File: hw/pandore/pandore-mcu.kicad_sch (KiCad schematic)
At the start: 33 parts, among them U3 RP2350B, U5 mem_flash_spi, X1 ${F}, ${tol}+${stab}, ${load}

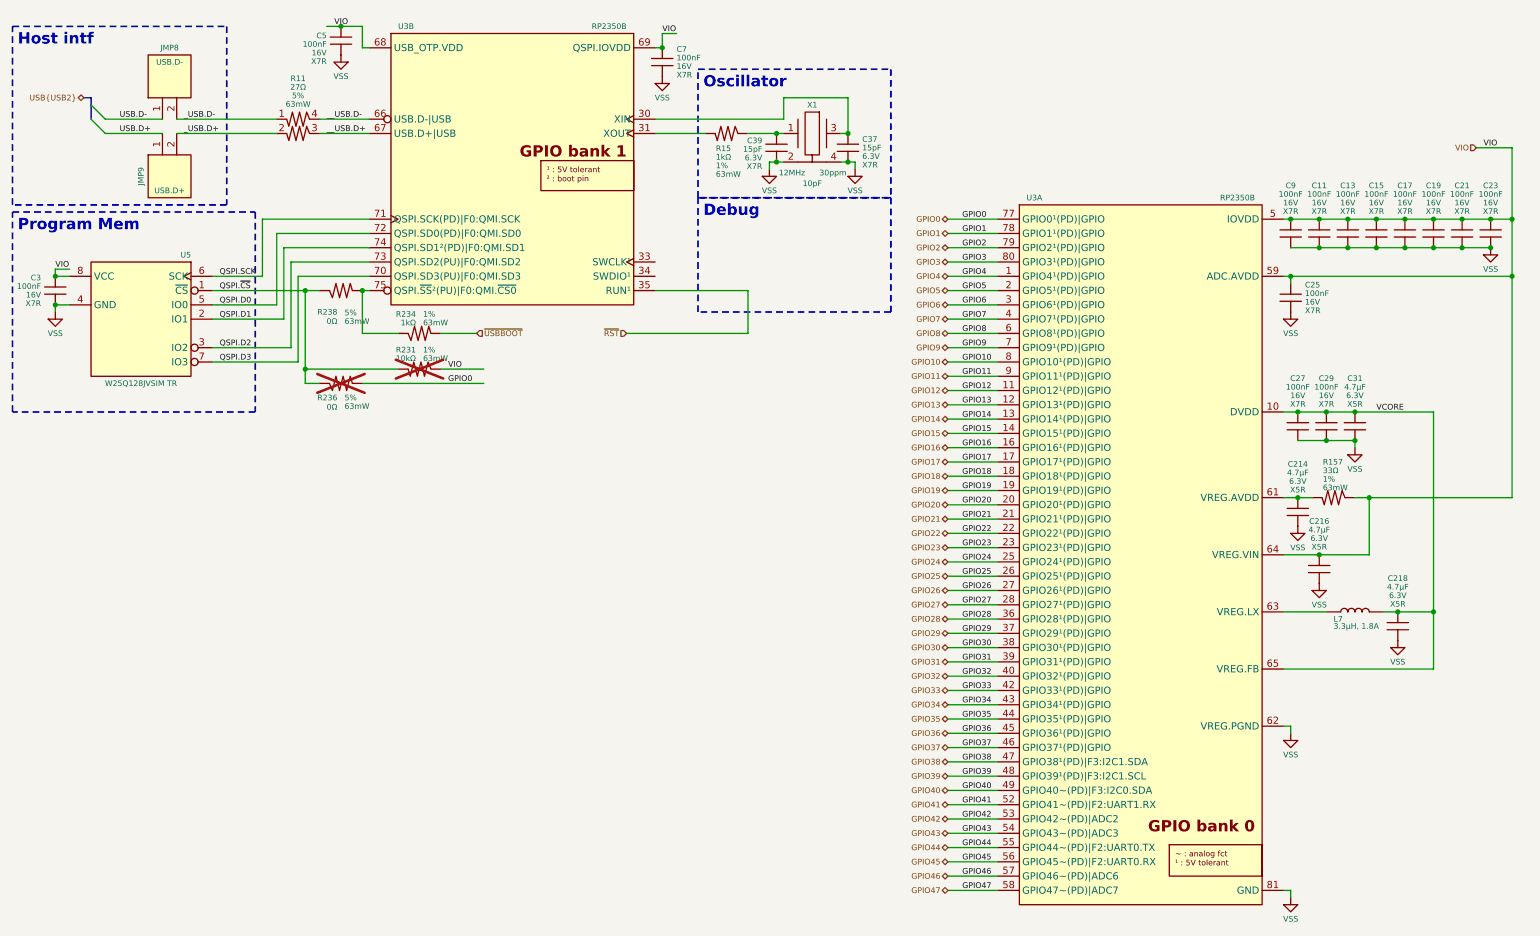
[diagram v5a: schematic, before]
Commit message: finished adding mpn,mfg to all parts, finished routing placement
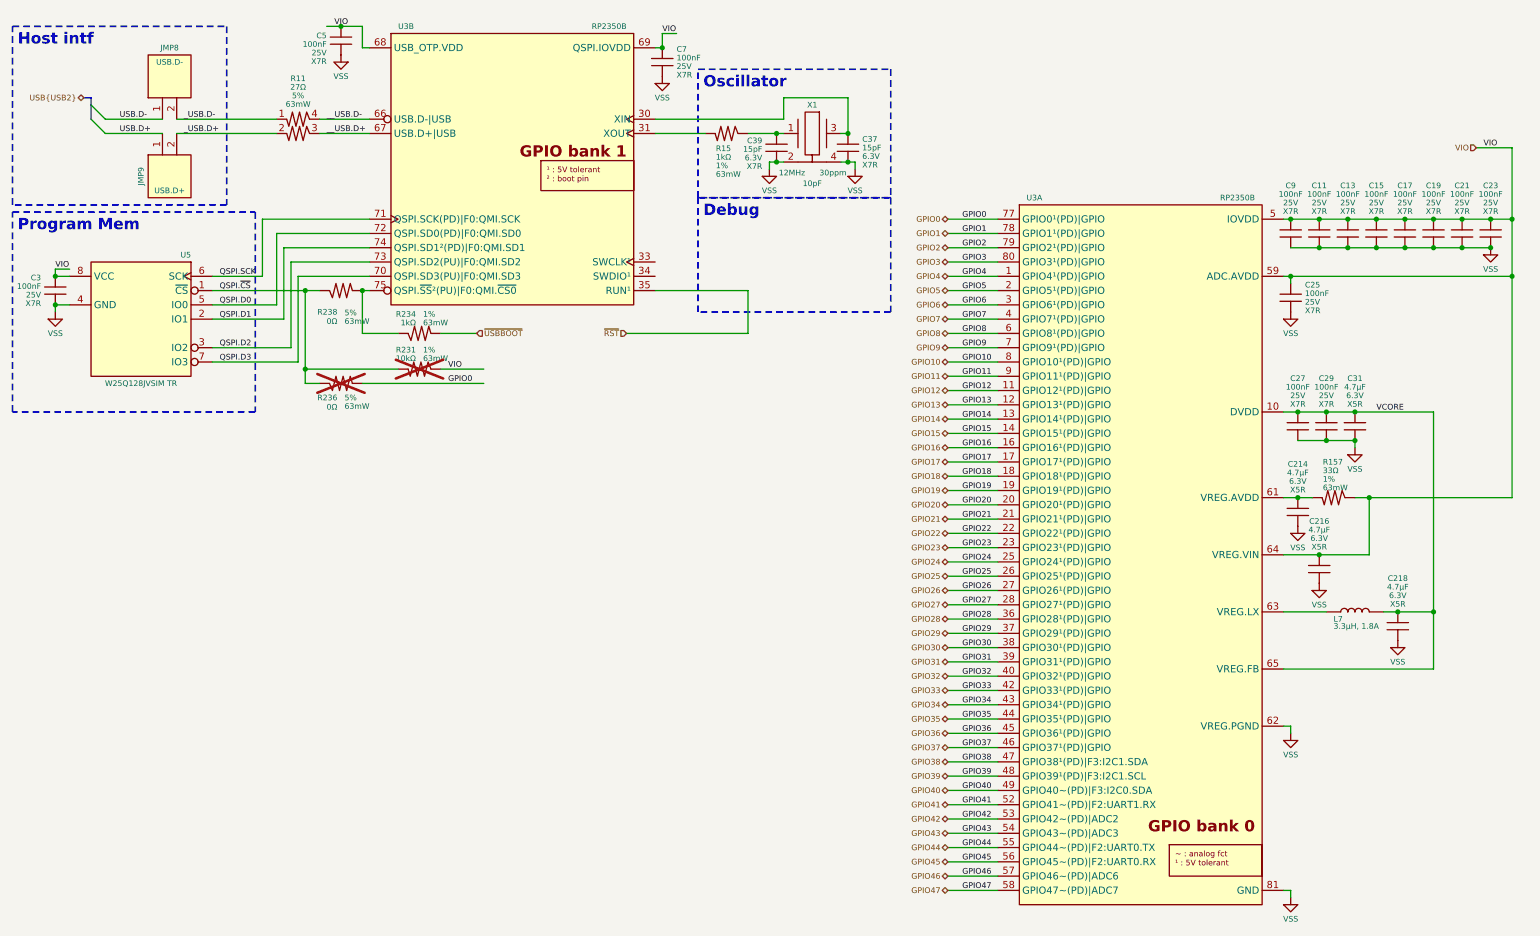
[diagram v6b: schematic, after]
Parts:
- C11, C13, C15, C17, C19, C21, C23, C25, C27, C29, C3, C5, C7, C9: MFG2 Samsung Electro-Mechanics -> (none); MFG3 Taiyo Yuden -> (none); MPN2 CL05B104KA5NNNC -> (none); MPN3 EMK105B7104KV-F -> (none); Voltage 16V -> 25V
- C37, C39: Link (none) -> https://yageogroup.com/products/Capacitors/part/CC0402JRNPO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; MFG (none) -> Yageo; MPN (none) -> CC0402JRNPO9BN150
- JMP8, JMP9: MFG (none) -> Adam Tech; MPN (none) -> PH1-02-UA
- R11: MFG (none) -> Panasonic Electronic Components; MPN (none) -> EXB-24V270JX
- R15, R234: Link (none) -> https://yageogroup.com/products/Resistors/part/RC0402FR-131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; MFG (none) -> YAGEO; MPN (none) -> RC0402FR-131KL
- R157: Link (none) -> https://yageogroup.com/products/Resistors/part/RC0402FR-073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; MFG (none) -> YAGEO; MPN (none) -> RC0402FR-0733RL
- R236, R238: Link (none) -> https://yageogroup.com/products/Resistors/part/RC0402JR-070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; MFG (none) -> Yageo; MFG2 (none) -> Stackpole; MFG3 (none) -> Vishay Dale; MPN (none) -> RC0402JR-070RL; MPN2 (none) -> RMCF0402ZT0R00; MPN3 (none) -> CRCW04020000Z0ED
